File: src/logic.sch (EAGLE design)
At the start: 66 parts, among them CON11 PINHEAD_1X03-2, CON12 PINHEAD_1X03-2, CON2 PINHEAD_2X02-PTH-2-MALE, CON3 PINHEAD_2X04-PLS-2, CON4 CON-3P-TABS, CON5 PINHEAD_2X02-PTH-2-MALE, CON6 PINHEAD_2X02-PTH-2-MALE, CON7 PINHEAD_2X02-PTH-2-MALE, IC1 STM32F105RCT6, IC10 LM75-TSSOP8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

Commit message: initial import
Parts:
- removed C10: 0.1µF, rc:C-0402
- removed C17, C18, C19, C20, C21, C23: 100µF, rc:CPOL-RADIAL_SIDE-12.5-22
- removed C28: 1µF, C_digikey:1µF-50V_10%_X7R-0603
- removed CON2, CON5: PINHEAD_2X02-PTH-2-MALE, pinhead:PINHEAD_2X02-PTH-2-MALE
- removed CON4: CON-3P-TABS, Connectors:CON-3P-TABS
- removed IC2: CAT24C02, misc:CAT24C02
- removed IC6: ZXCT1051, misc:ZXCT1051
- removed R12: 3K9, R_digikey:3K9-1%-0402
- added C14: 0.1µF, rc:C-0402
- added CON1: CON-4P-TABS-JST_GH-RA, Connectors:CON-4P-TABS-JST_GH-RA
- added IC5: INA180A1, misc:INA180A1
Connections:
- removed net BLABLA: IC6.VOUT, R12.1
- removed net VBAT: C17.+, C18.+, C19.+, C20.+, C21.+, C23.+
- new net CS+: CON3.7
- new net CS-: CON3.5
- new net N$5: IC5.IN+
- new net N$8: IC5.IN-
- new net RCPWM: CON1.1
- new net VBAT-: CON3.3
- new net VDC: CON3.1
- new net VDD_12V: CON3.6, CON6.1, CON7.1
- net FET_A_H: now also CON6.2
- net FET_A_L: now also CON6.4
- net FET_C_H: now also CON3.2, CON7.2
- net FET_C_L: now also CON3.4, CON7.4
- net GND: now also C14.2, CON1.4, CON1.GND, IC5.GND; no longer C10.2, C17.-, C18.-, C19.-, C20.-, C21.-, C23.-, C28.1, CON4.3, CON4.GND, IC2.VSS, IC6.GND
- net I2C_SCL: no longer IC2.SCL
- net I2C_SDA: no longer IC2.SDA
- net N$1: no longer IC6.VSENSE-
- net N$2: no longer IC6.VSENSE+
- net N$29: now also CON1.3; no longer CON4.2
- net N$30: now also CON1.2; no longer CON4.1
- net PHASE_A: now also CON6.3
- net PHASE_B: now also CON7.3
- net PHASE_C: now also CON3.8
- net SENSE_CURRENT: now also IC5.OUT; no longer C28.2, R12.2
- net VDD_3V3: now also C14.1, IC5.VS; no longer C10.1, IC2.VCC, IC6.VCC
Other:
- note removed: "Should replace IC6 with INA213 from TI"
- moved on the sheet: CON3, CON6, CON7

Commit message: Connectors update
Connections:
- removed net N$5: IC5.IN+
- removed net N$8: IC5.IN-
- net CS+: now also IC5.IN+
- net CS-: now also IC5.IN-
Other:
- moved on the sheet: C14, CON3, CON6, CON7, IC5

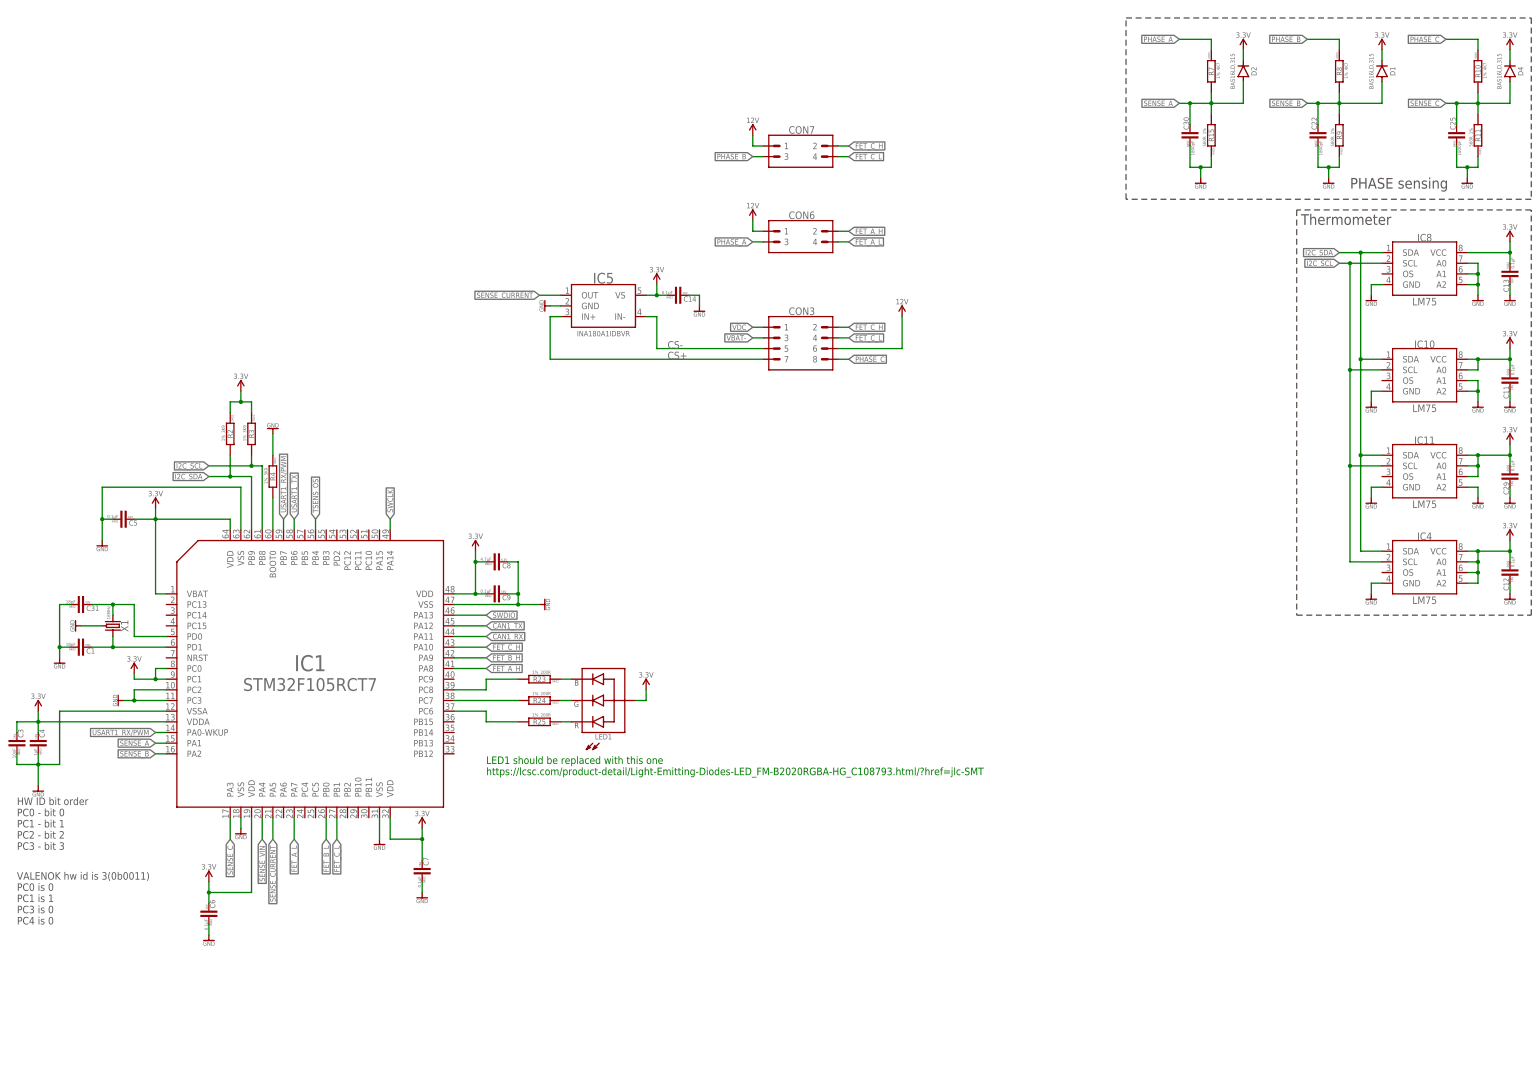
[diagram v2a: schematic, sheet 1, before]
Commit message: Components placement
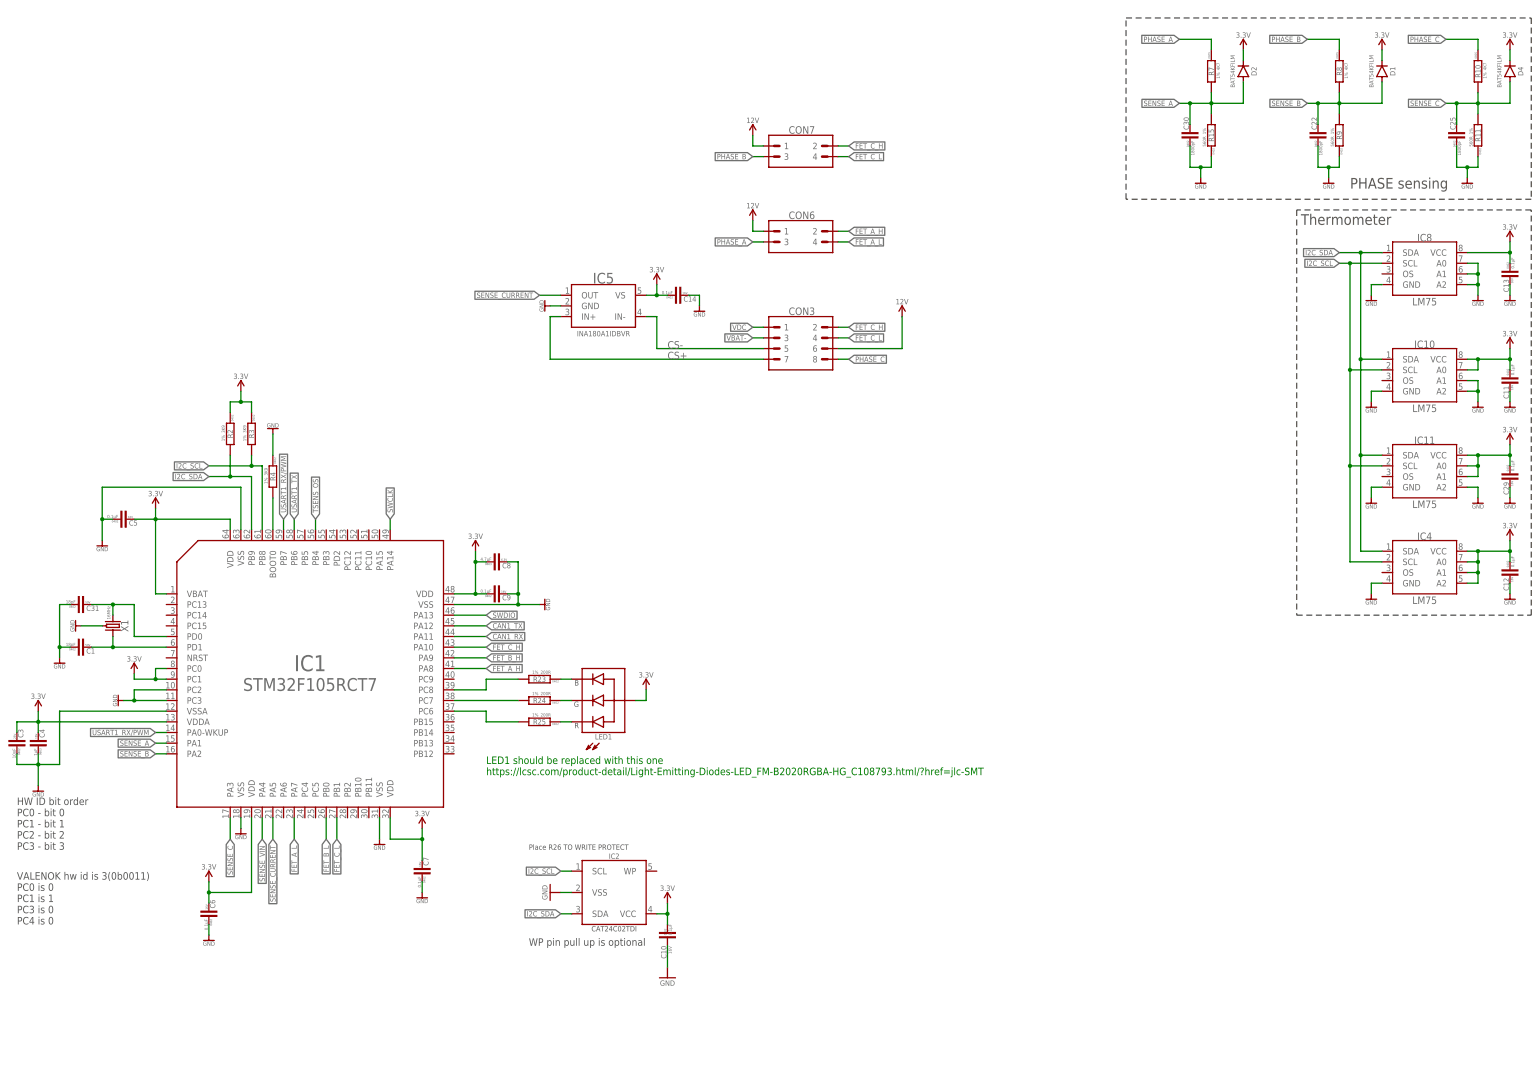
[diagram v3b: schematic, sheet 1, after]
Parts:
- added C10: 0.1µF, C_digikey:0.1µF-16V_10%_X7R-0402
- added IC2: CAT24C02, misc:CAT24C02
- added R1: 000, rc:R-1%-0805
- D1, D2, D4: value BAS16L -> BAT54KFILM; device Diodes:BAS16L -> Diodes:BAT54KFILM
- X1: device crystal:CRYSTAL-4P-16MHZ-2.0X1.6 -> crystal:CRYSTAL-4P-16MHZ-3.2X2.5
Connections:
- new net FB: IC1.FB, R1.1, R2.2
- net GND: now also C10.2, IC2.VSS, R2.1; no longer IC1.FB
- net I2C_SCL: now also IC2.SCL
- net I2C_SDA: now also IC2.SDA
- net OUT: now also R1.2
- net VDD_3V3: now also C10.1, IC2.VCC, R1.2
- net VDD_5V: now also R1.1
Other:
- note added: "Place R26 TO WRITE PROTECT"
- note added: "WP pin pull up is optional"

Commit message: Updates here and there
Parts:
- removed LED1: LTST-C19HE1WT, misc:LTST-C19HE1WT
- added C15: 0.1µF, rc:C-0402
- added LED2: LED_RGB-2020, rc:LED_RGB-2020
- added R5: (no value), rc:R-1%-0805
- added R6: (no value), rc:R-1%-0402
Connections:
- removed net USART1_RX/PWM: IC1.PA0-WKUP, IC1.PB7, IC7.R1OUT
- removed net VBAT-: CON3.3
- new net RC_PWM: IC1.PA0-WKUP
- new net USART1_RX: IC1.PB7, IC7.R1OUT
- net FET_A_H: now also CON3.2; no longer CON6.2
- net FET_A_L: now also CON3.4; no longer CON6.4
- net FET_B_H: now also CON7.2
- net FET_B_L: now also CON7.4
- net FET_C_H: now also CON6.2; no longer CON3.2, CON7.2
- net FET_C_L: now also CON6.4; no longer CON3.4, CON7.4
- net GND: now also C15.1, CON3.3, R6.1
- net N$26: now also LED2.G; no longer LED1.G
- net N$6: now also LED2.B; no longer LED1.B
- net N$7: now also LED2.R; no longer LED1.R
- net PHASE_A: now also CON3.8, R10.1; no longer CON6.3, R7.1
- net PHASE_C: now also CON6.3, R7.1; no longer CON3.8, R10.1
- net SENSE_A: now also C25.2, D4.A, R10.2, R11.2; no longer C30.2, D2.A, R15.2, R7.2
- net SENSE_C: now also C30.2, D2.A, R15.2, R7.2; no longer C25.2, D4.A, R10.2, R11.2
- net SENSE_VIN: now also C15.2, R5.1, R6.2
- net VDC: now also R5.2
- net VDD_3V3: now also LED2.A; no longer LED1.A
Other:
- moved on the sheet: CON6, CON7

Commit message: routing upodates
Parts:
- added CON2: PINHEAD_1X04-2.54, pinhead:PINHEAD_1X04-2.54
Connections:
- net GND: now also CON2.3
- net SWCLK: now also CON2.1
- net SWDIO: now also CON2.2
- net VDD_3V3: now also CON2.4
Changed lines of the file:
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@@
 <part name="+P10" library="supply_symbols" library_urn="urn:adsk.eagle:library:5017758" deviceset="VDC" device=""/>
 <part name="+P13" library="supply_symbols" library_urn="urn:adsk.eagle:library:5017758" deviceset="VDC" device=""/>
+<part name="CON2" library="pinhead" library_urn="urn:adsk.eagle:library:2540341" deviceset="PINHEAD_1X04" device="-2.54" package3d_urn="urn:adsk.eagle:package:2540383/2"/>
+<part name="GND23" library="supply_symbols" library_urn="urn:adsk.eagle:library:13097679" deviceset="GND" device="" value="GND"/>
+<part name="P+15" library="supply_symbols" library_urn="urn:adsk.eagle:library:13097679" deviceset="3.3V" device=""/>
 </parts>
 <sheets>
@@
 <attribute name="VALUE" x="271.78" y="181.356" size="1.27" layer="96" font="vector" ratio="15" align="center"/>
 </instance>
+<instance part="CON2" gate="G$1" x="167.64" y="134.62" smashed="yes" rot="MR0">
+<attribute name="NAME" x="165.1" y="148.59" size="1.778" layer="95" font="vector" ratio="15" rot="MR0" align="center"/>
+</instance>
+<instance part="GND23" gate="1" x="154.94" y="142.24" smashed="yes" rot="R270">
+<attribute name="VALUE" x="152.908" y="142.24" size="1.016" layer="96" font="vector" ratio="15" rot="R270" align="center"/>
+</instance>
+<instance part="P+15" gate="G$1" x="154.94" y="147.32" smashed="yes">
+<attribute name="VALUE" x="154.94" y="150.876" size="1.27" layer="96" font="vector" ratio="15" align="center"/>
+</instance>
 </instances>
 <busses>
@@
 <label x="132.08" y="111.76" size="1.27" layer="95" xref="yes"/>
 </segment>
+<segment>
+<pinref part="CON2" gate="G$1" pin="2"/>
+<wire x1="160.02" y1="139.7" x2="157.48" y2="139.7" width="0.1524" layer="91"/>
+<label x="157.48" y="139.7" size="1.27" layer="95" rot="R180" xref="yes"/>
+</segment>
 </net>
 <net name="SWCLK" class="0">
@@
 <wire x1="109.22" y1="132.08" x2="109.22" y2="134.62" width="0.1524" layer="91"/>
 <label x="109.22" y="134.62" size="1.27" layer="95" rot="R90" xref="yes"/>
+</segment>
+<segment>
+<pinref part="CON2" gate="G$1" pin="1"/>
+<wire x1="160.02" y1="137.16" x2="157.48" y2="137.16" width="0.1524" layer="91"/>
+<label x="157.48" y="137.16" size="1.27" layer="95" rot="R180" xref="yes"/>
 </segment>
 </net>
@@
 <wire x1="271.78" y1="144.78" x2="271.78" y2="147.32" width="0.1524" layer="91"/>
 <junction x="271.78" y="147.32"/>
+</segment>
+<segment>
+<pinref part="CON2" gate="G$1" pin="3"/>
+<pinref part="GND23" gate="1" pin="GND"/>
+<wire x1="160.02" y1="142.24" x2="154.94" y2="142.24" width="0.1524" layer="91"/>
 </segment>
 </net>
@@
 <pinref part="P+10" gate="G$1" pin="VDD_3V3"/>
 </segment>
-</net>
+<segment>
+<pinref part="CON2" gate="G$1" pin="4"/>
+<wire x1="160.02" y1="144.78" x2="154.94" y2="144.78" width="0.1524" layer="91"/>
+<pinref part="P+15" gate="G$1" pin="VDD_3V3"/>
+<wire x1="154.94" y1="144.78" x2="154.94" y2="147.32" width="0.1524" layer="91"/>
+</segment>
+</net>

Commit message: Currennt measurement update
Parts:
- added C16: 0.1µF, rc:C-0402
- added IC6: LMV331, misc:LMV331
- added R12: 3K9, rc:R-1%-0402
- added R14: DNM, rc:R-1%-0402
- added R16, R17: 000, rc:R-1%-0402
- IC5: value INA180A1 -> INA180A2; device misc:INA180A1 -> misc:INA180A2
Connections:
- removed net SENSE_CURRENT: IC1.PA5, IC5.OUT
- new net CURRENT_AMP_OUT: IC1.PA5, IC5.OUT, IC6.IN-
- new net OVERCURRENT_FAULT: IC6.OUT, R12.2, R14.1
- net GND: now also C16.1, IC6.V-, R17.2
- net N$2: now also IC6.IN+, R14.2, R16.1, R17.1
- net VDD_3V3: now also C16.2, IC6.V+, R12.1, R16.2
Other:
- note added: "Inverting comparator"
- note added: "When current_amp_out voltage exceeds comp_ref voltage overcurrent_fault goes low"
- moved on the sheet: C14, IC5
